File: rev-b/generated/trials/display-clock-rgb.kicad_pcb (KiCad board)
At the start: 4 copper layers, 136 x 106 mm, 351 parts, among them J1001 LCD RGB / contact fit pending, J1002 CAP TOUCH / contact fit pendi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, J1101 FOOT WIRE: 1SIGNAL 2GND, J1102 FOOT WIRE: 1SIGNAL 2GND, J201 NMJ4HCD2 INPUT, J202 NMJ4HCD2 OUTPUT, J401 PJ-102AH, J501 GOWIN JTAG / target VREF only, J701 UART / POWERED TARGET ONLY, Q401 AO4407A, SW501 RECONFIG / MPN pending, SW701 RESET / SMD button MPN pending, SW702 BOOT / SMD button MPN pending, U101 TPS54302DDCR, U102 TPS54302DDCR, U1101 SN74LVC1G17DCKR, U1102 SN74LVC1G17DCKR, U201 PCM1808PWR, U202 PCM5102APWR, U203 OPA1656IDR, U204 TLV76750DRVR, U205 TLV75533PDBVR, U206 TPS3808G01DBVR, U207 TPS3808G01DBVR, U301 TLV62569DBVR, U302 TPS3897ADRYR, U303 TPS22965DSGR, U501 GW2AR-LV18QN88C8/I7, U502 GD25Q32ESIGR, U503 SN74LVC1G125DCKR, U504 SN74LVC1G17DCKR, U601 TLV62569DBVR, U701 ESP32-P4NRW16X, U702 GD25Q32ESIGR, U801 SN74AXC4T774PWR, U802 TPS3808G01DBVR, U803 SN74LVC1G00DCKR, U901 TPS61169DCKR, U902 SN74LVC1G125DCKR, U903 TLV76701DRVR, U904 TLV76701DRVR, Y501 24.576MHz / 3.3V CMOS XO / MP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, Y701 40MHz / +/-10ppm / MPN and CL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

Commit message: Route touch SCL and guard all timing outputs in coordinated trial
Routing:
- net /RGB565 and capacitive touch/TOUCH_SCL: track 5.96 -> 58.2 mm, vias 2 -> 6
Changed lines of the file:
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@@
+	)
+	(segment
+		(start 141.45 62.9)
+		(end 146.35 58)
+		(width 0.127)
+		(layer "F.Cu")
+		(net "/RGB565 and capacitive touch/TOUCH_SCL")
+	)
+	(segment
+		(start 149.05 58.1)
+		(end 149.5 58.1)
+		(width 0.127)
+		(layer "F.Cu")
+		(net "/RGB565 and capacitive touch/TOUCH_SCL")
+	)
+	(segment
+		(start 149.5 58.1)
+		(end 150.75 56.85)
+		(width 0.127)
+		(layer "F.Cu")
+		(net "/RGB565 and capacitive touch/TOUCH_SCL")
+	)
+	(segment
+		(start 125.7 69.15)
+		(end 125.7 66.8)
+		(width 0.127)
+		(layer "F.Cu")
+		(net "/RGB565 and capacitive touch/TOUCH_SCL")
+	)
+	(segment
+		(start 146.35 58)
+		(end 148.95 58)
+		(width 0.127)
+		(layer "F.Cu")
+		(net "/RGB565 and capacitive touch/TOUCH_SCL")
 	)
 	(segment
@@
 	)
 	(segment
+		(start 150.75 56.85)
+		(end 150.75 56.15)
+		(width 0.127)
+		(layer "F.Cu")
+		(net "/RGB565 and capacitive touch/TOUCH_SCL")
+	)
+	(segment
 		(start 150.75 56.15)
 		(end 150.75 55.1)
+		(width 0.127)
+		(layer "F.Cu")
+		(net "/RGB565 and capacitive touch/TOUCH_SCL")
+	)
+	(segment
+		(start 148.95 58)
+		(end 149.05 58.1)
+		(width 0.127)
+		(layer "F.Cu")
+		(net "/RGB565 and capacitive touch/TOUCH_SCL")
+	)
+	(segment
+		(start 125.7 66.8)
+		(end 129.6 62.9)
 		(width 0.127)
 		(layer "F.Cu")
@@
 	)
 	(via
+		(at 125.7 69.15)
+		(size 0.5)
+		(drill 0.3)
+		(layers "F.Cu" "B.Cu")
+		(net "/RGB565 and capacitive touch/TOUCH_SCL")
+	)
+	(via
 		(at 147.325 52)
 		(size 0.5)
@@
 		(net "/RGB565 and capacitive touch/TOUCH_SCL")
 	)
+	(via
+		(at 114.7 80.15)
+		(size 0.5)
+		(drill 0.3)
+		(layers "F.Cu" "B.Cu")
+		(net "/RGB565 and capacitive touch/TOUCH_SCL")
+	)
+	(via
+		(at 129.6 62.9)
+		(size 0.5)
+		(drill 0.3)
+		(layers "F.Cu" "B.Cu")
+		(net "/RGB565 and capacitive touch/TOUCH_SCL")
+	)
+	(via
+		(at 141.45 62.9)
+		(size 0.5)
+		(drill 0.3)
+		(layers "F.Cu" "B.Cu")
+		(net "/RGB565 and capacitive touch/TOUCH_SCL")
+	)
+	(segment
+		(start 114.7 84.49)
+		(end 114.7 80.15)
+		(width 0.127)
+		(layer "B.Cu")
+		(net "/RGB565 and capacitive touch/TOUCH_SCL")
+	)
+	(segment
+		(start 129.6 62.9)
+		(end 141.45 62.9)
+		(width 0.127)
+		(layer "In2.Cu")
+		(net "/RGB565 and capacitive touch/TOUCH_SCL")
+	)
+	(segment
+		(start 114.7 80.15)
+		(end 125.7 69.15)
+		(width 0.127)
+		(layer "In2.Cu")
+		(net "/RGB565 and capacitive touch/TOUCH_SCL")
+	)

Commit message: Route LCD DE and record checked touch source reservation limits
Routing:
- net /RGB565 and capacitive touch/LCD_DE: track 0.00 -> 62.3 mm, vias 0 -> 3
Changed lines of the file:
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@@
+	)
+	(segment
+		(start 124.55 55.2)
+		(end 123.75 54.4)
+		(width 0.127)
+		(layer "F.Cu")
+		(net "/RGB565 and capacitive touch/LCD_DE")
+	)
+	(segment
+		(start 125.3 55.2)
+		(end 124.55 55.2)
+		(width 0.127)
+		(layer "F.Cu")
+		(net "/RGB565 and capacitive touch/LCD_DE")
+	)
+	(segment
+		(start 123.75 54.4)
+		(end 123.75 53.15)
+		(width 0.127)
+		(layer "F.Cu")
+		(net "/RGB565 and capacitive touch/LCD_DE")
+	)
+	(segment
+		(start 129.55 92.3)
+		(end 130 92.75)
+		(width 0.127)
+		(layer "F.Cu")
+		(net "/RGB565 and capacitive touch/LCD_DE")
+	)
+	(segment
+		(start 130 92.75)
+		(end 130.5 92.75)
+		(width 0.127)
+		(layer "F.Cu")
+		(net "/RGB565 and capacitive touch/LCD_DE")
+	)
+	(segment
+		(start 130.5 92.75)
+		(end 131.699999 91.55)
+		(width 0.127)
+		(layer "F.Cu")
+		(net "/RGB565 and capacitive touch/LCD_DE")
+	)
+	(segment
+		(start 127.05 92.3)
+		(end 129.55 92.3)
+		(width 0.127)
+		(layer "F.Cu")
+		(net "/RGB565 and capacitive touch/LCD_DE")
+	)
+	(segment
+		(start 131.699999 91.55)
+		(end 133.199999 91.55)
+		(width 0.127)
+		(layer "F.Cu")
+		(net "/RGB565 and capacitive touch/LCD_DE")
+	)
+	(via
+		(at 127.05 92.3)
+		(size 0.5)
+		(drill 0.3)
+		(layers "F.Cu" "B.Cu")
+		(net "/RGB565 and capacitive touch/LCD_DE")
+	)
+	(via
+		(at 125.3 55.2)
+		(size 0.5)
+		(drill 0.3)
+		(layers "F.Cu" "B.Cu")
+		(net "/RGB565 and capacitive touch/LCD_DE")
+	)
+	(via
+		(at 133.199999 91.55)
+		(size 0.5)
+		(drill 0.3)
+		(layers "F.Cu" "B.Cu")
+		(net "/RGB565 and capacitive touch/LCD_DE")
+	)
+	(segment
+		(start 123.4 88.65)
+		(end 127.05 92.3)
+		(width 0.127)
+		(layer "B.Cu")
+		(net "/RGB565 and capacitive touch/LCD_DE")
+	)
+	(segment
+		(start 121.35 87.8)
+		(end 123.05 87.8)
+		(width 0.127)
+		(layer "B.Cu")
+		(net "/RGB565 and capacitive touch/LCD_DE")
+	)
+	(segment
+		(start 135.75 89)
+		(end 135.75 65.7)
+		(width 0.127)
+		(layer "B.Cu")
+		(net "/RGB565 and capacitive touch/LCD_DE")
+	)
+	(segment
+		(start 119.5 85.8)
+		(end 119.5 85.95)
+		(width 0.127)
+		(layer "B.Cu")
+		(net "/RGB565 and capacitive touch/LCD_DE")
+	)
+	(segment
+		(start 133.199999 91.55)
+		(end 135.75 89)
+		(width 0.127)
+		(layer "B.Cu")
+		(net "/RGB565 and capacitive touch/LCD_DE")
+	)
+	(segment
+		(start 123.05 87.8)
+		(end 123.4 88.15)
+		(width 0.127)
+		(layer "B.Cu")
+		(net "/RGB565 and capacitive touch/LCD_DE")
+	)
+	(segment
+		(start 135.75 65.7)
+		(end 125.3 55.25)
+		(width 0.127)
+		(layer "B.Cu")
+		(net "/RGB565 and capacitive touch/LCD_DE")
+	)
+	(segment
+		(start 119.5 85.95)
+		(end 121.35 87.8)
+		(width 0.127)
+		(layer "B.Cu")
+		(net "/RGB565 and capacitive touch/LCD_DE")
+	)
+	(segment
+		(start 125.3 55.25)
+		(end 125.3 55.2)
+		(width 0.127)
+		(layer "B.Cu")
+		(net "/RGB565 and capacitive touch/LCD_DE")
+	)
+	(segment
+		(start 119.51 85.8)
+		(end 119.5 85.8)
+		(width 0.127)
+		(layer "B.Cu")
+		(net "/RGB565 and capacitive touch/LCD_DE")
+	)
+	(segment
+		(start 123.4 88.15)
+		(end 123.4 88.65)
+		(width 0.127)
+		(layer "B.Cu")
+		(net "/RGB565 and capacitive touch/LCD_DE")
 	)
 	(segment

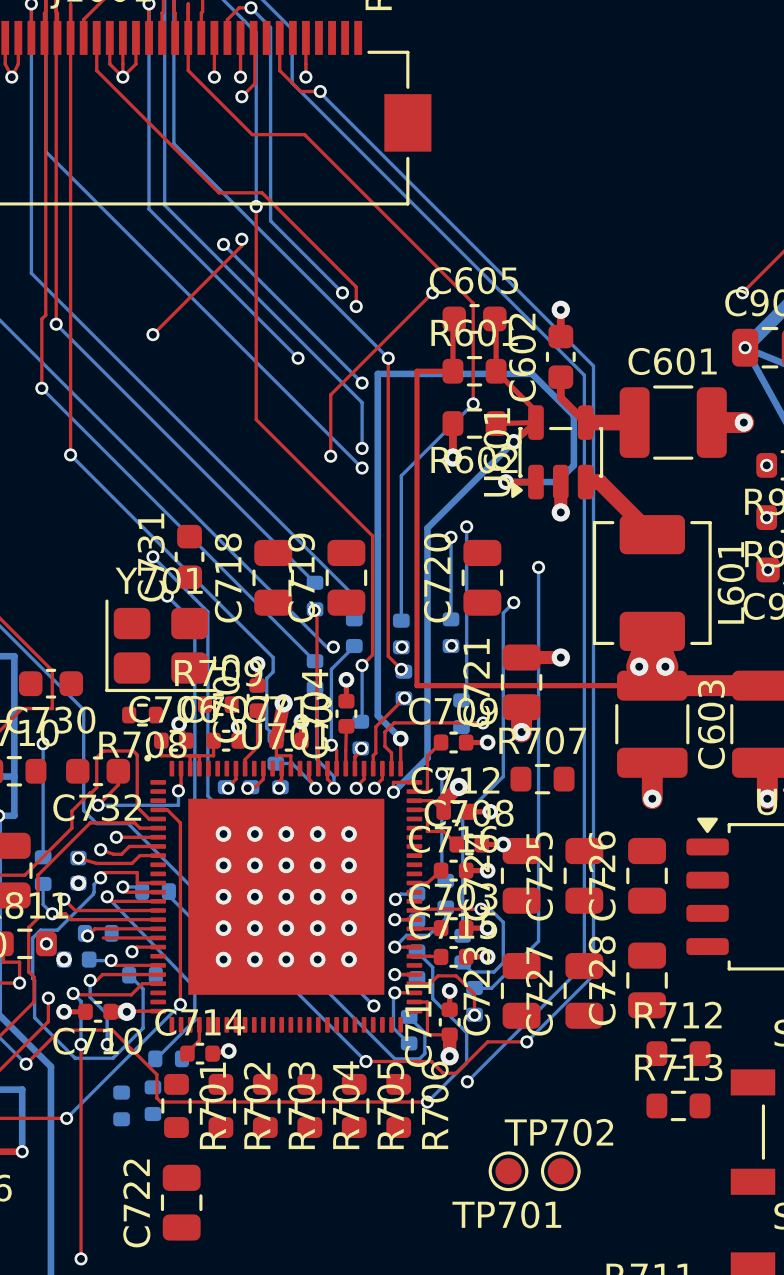
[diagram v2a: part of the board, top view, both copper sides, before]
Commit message: Route LCD DISP using existing via and enforce drill spacing in proposals
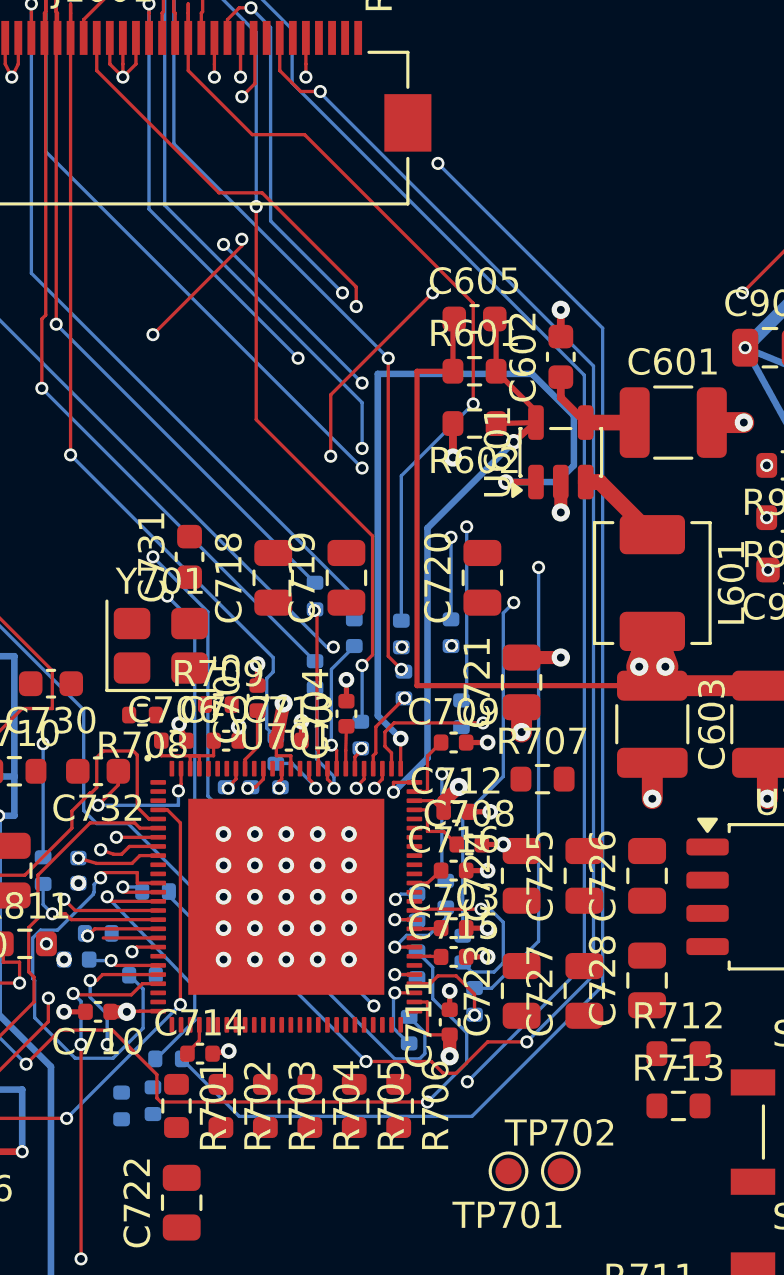
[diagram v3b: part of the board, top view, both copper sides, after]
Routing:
- net /RGB565 and capacitive touch/LCD_DISP: track 9.26 -> 71.3 mm, vias 2 -> 3
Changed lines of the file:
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@@
+		(net "/RGB565 and capacitive touch/LCD_DISP")
+	)
+	(via
+		(at 129.8 57.95)
+		(size 0.5)
+		(drill 0.3)
+		(layers "F.Cu" "B.Cu")
+		(net "/RGB565 and capacitive touch/LCD_DISP")
+	)
+	(segment
+		(start 120 92.2)
+		(end 122.2 94.4)
+		(width 0.127)
+		(layer "B.Cu")
+		(net "/RGB565 and capacitive touch/LCD_DISP")
+	)
+	(segment
+		(start 122.2 94.4)
+		(end 131.1 94.4)
+		(width 0.127)
+		(layer "B.Cu")
+		(net "/RGB565 and capacitive touch/LCD_DISP")
+	)
+	(segment
+		(start 131.1 94.4)
+		(end 136.1 89.4)
+		(width 0.127)
+		(layer "B.Cu")
+		(net "/RGB565 and capacitive touch/LCD_DISP")
+	)
+	(segment
+		(start 120.01 92.2)
+		(end 120 92.2)
+		(width 0.127)
+		(layer "B.Cu")
+		(net "/RGB565 and capacitive touch/LCD_DISP")
+	)
+	(segment
+		(start 136.1 64.25)
+		(end 129.8 57.95)
+		(width 0.127)
+		(layer "B.Cu")
+		(net "/RGB565 and capacitive touch/LCD_DISP")
+	)
+	(segment
+		(start 136.1 89.4)
+		(end 136.1 64.25)
+		(width 0.127)
+		(layer "B.Cu")
+		(net "/RGB565 and capacitive touch/LCD_DISP")
+	)
+	(segment
+		(start 125.6 57.95)
+		(end 122.3 54.65)
+		(width 0.127)
+		(layer "In2.Cu")
+		(net "/RGB565 and capacitive touch/LCD_DISP")
+	)
+	(segment
+		(start 122.3 54.65)
+		(end 122.25 54.65)
+		(width 0.127)
+		(layer "In2.Cu")
+		(net "/RGB565 and capacitive touch/LCD_DISP")
+	)
+	(segment
+		(start 129.8 57.95)
+		(end 125.6 57.95)
+		(width 0.127)
+		(layer "In2.Cu")
 		(net "/RGB565 and capacitive touch/LCD_DISP")
 	)
